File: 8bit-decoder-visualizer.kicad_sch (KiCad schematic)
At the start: 24 parts, among them U1 LED Display Module, U2 LED Display Module, U3 LED Display Module, U4 LED Display Module, U5 LED Display Module, U6 LED Display Module, U7 74HC595

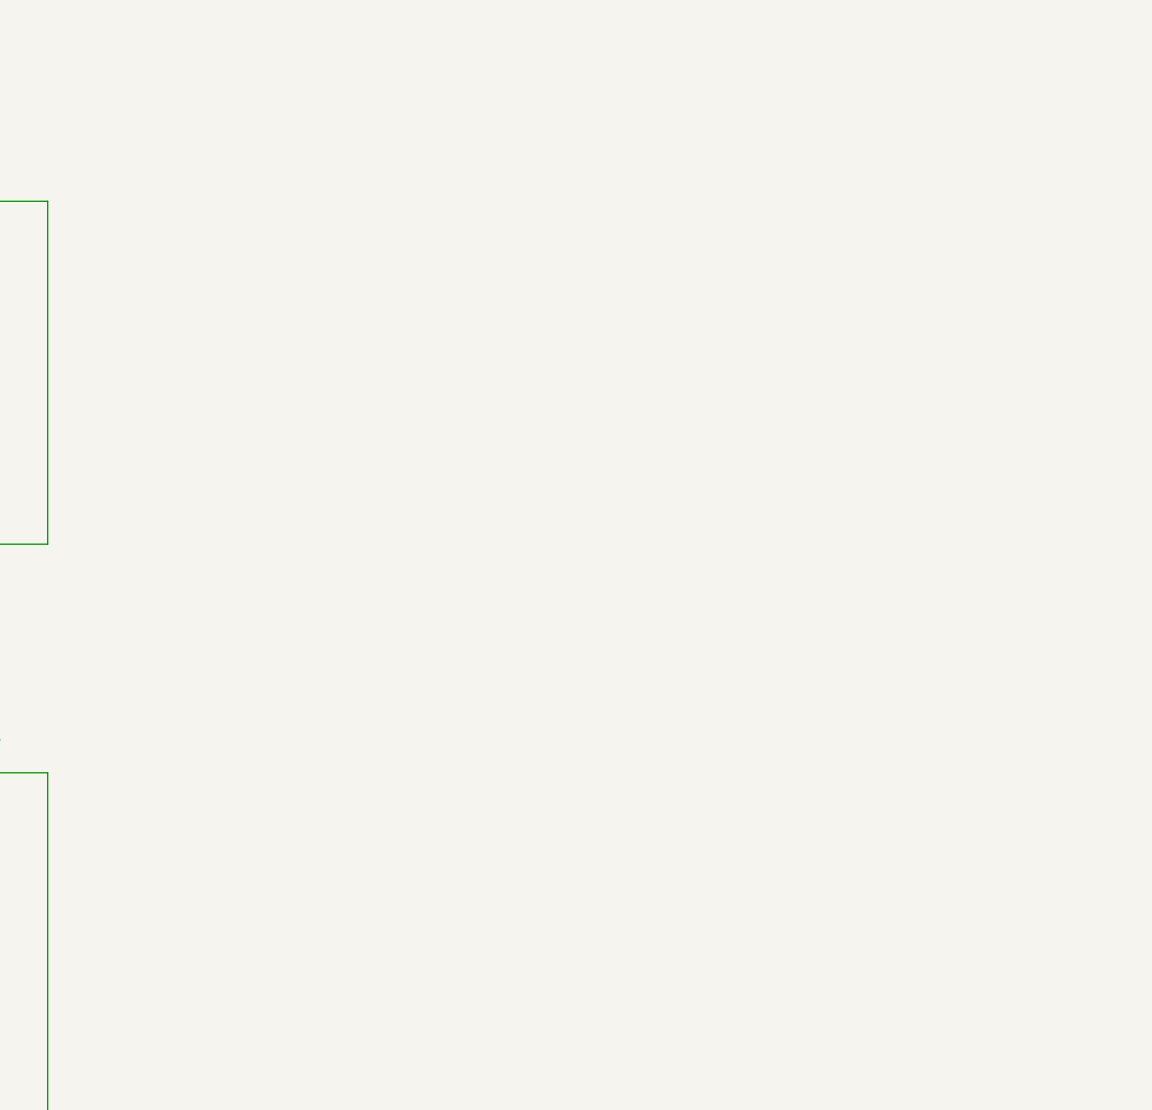
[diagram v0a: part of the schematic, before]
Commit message: xiao との接続以外の回路を書いた
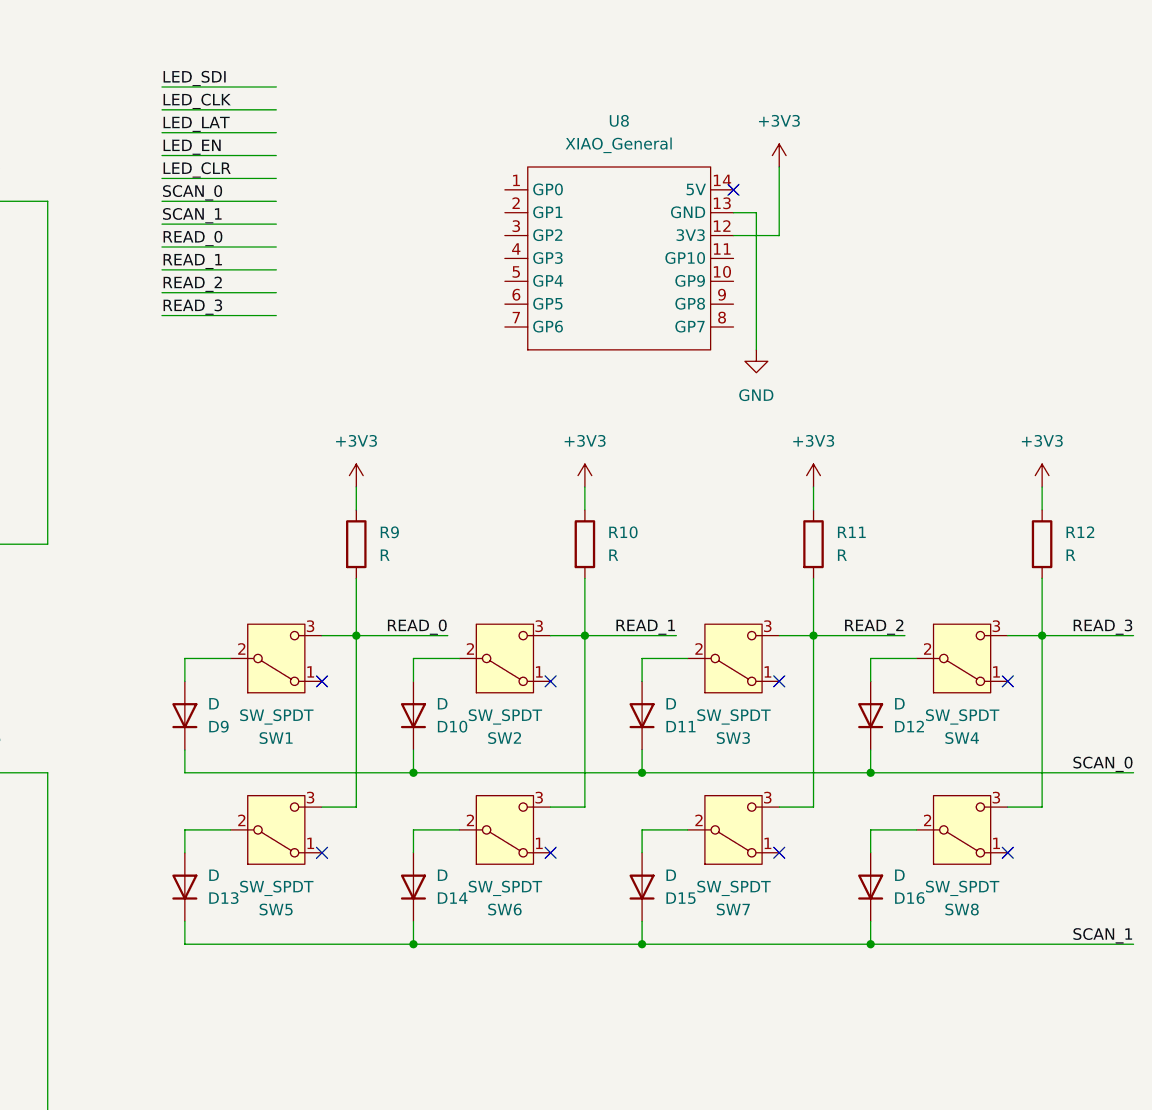
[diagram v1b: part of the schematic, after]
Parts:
- added D10, D11, D12, D13, D14, D15, D16, D9: D, symbol Device:D
- added R10, R11, R12, R9: R, Resistor_SMD:R_0603_1608Metric, symbol Device:R
- added SW1, SW2, SW3, SW4, SW5, SW6, SW7, SW8: SW_SPDT, Button_Switch_THT:SW_Slide_SPDT_Straight_CK_OS102011MS2Q, symbol Switch:SW_SPDT
- added U8: XIAO_General, board:XIAO_ESP32_C3, symbol board:XIAO_General
- U7: footprint (none) -> Package_DIP:DIP-16_W7.62mm
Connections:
- net +3V3: now also R10.1, R11.1, R12.1, R9.1, U8.12 (3V3)
- net GND: now also U8.13 (GND)
- new net: D11.2 (A), SW3.2 (B)
- new net: D12.2 (A), SW4.2 (B)
- new net: D10.2 (A), SW2.2 (B)
- new net: D14.2 (A), SW6.2 (B)
- new net: D15.2 (A), SW7.2 (B)
- new net: D13.2 (A), SW5.2 (B)
- new net: D16.2 (A), SW8.2 (B)
- new net: D9.2 (A), SW1.2 (B)
- new net READ_0: R9.2, SW1.3 (C), SW5.3 (C)
- new net READ_1: R10.2, SW2.3 (C), SW6.3 (C)
- new net READ_2: R11.2, SW3.3 (C), SW7.3 (C)
- new net READ_3: R12.2, SW4.3 (C), SW8.3 (C)
- new net SCAN_0: D10.1 (K), D11.1 (K), D12.1 (K), D9.1 (K)
- new net SCAN_1: D13.1 (K), D14.1 (K), D15.1 (K), D16.1 (K)
- no-connect marks 1 -> 10

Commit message: フットプリントの割り当てを忘れてたでヤンス
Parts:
- D10, D11, D12, D13, D14, D15, D16, D9: footprint (none) -> Diode_SMD:D_SOD-123F
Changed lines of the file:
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@@
 			)
 		)
-		(property "Footprint" ""
+		(property "Footprint" "Diode_SMD:D_SOD-123F"
 			(at 243.84 95.25 0)
 			(effects
@@
 			)
 		)
-		(property "Footprint" ""
+		(property "Footprint" "Diode_SMD:D_SOD-123F"
 			(at 193.04 95.25 0)
 			(effects
@@
 			)
 		)
-		(property "Footprint" ""
+		(property "Footprint" "Diode_SMD:D_SOD-123F"
 			(at 193.04 114.3 0)
 			(effects
@@
 			)
 		)
-		(property "Footprint" ""
+		(property "Footprint" "Diode_SMD:D_SOD-123F"
 			(at 167.64 114.3 0)
 			(effects
@@
 			)
 		)
-		(property "Footprint" ""
+		(property "Footprint" "Diode_SMD:D_SOD-123F"
 			(at 218.44 95.25 0)
 			(effects
@@
 			)
 		)
-		(property "Footprint" ""
+		(property "Footprint" "Diode_SMD:D_SOD-123F"
 			(at 218.44 114.3 0)
 			(effects
@@
 			)
 		)
-		(property "Footprint" ""
+		(property "Footprint" "Diode_SMD:D_SOD-123F"
 			(at 243.84 114.3 0)
 			(effects
@@
 			)
 		)
-		(property "Footprint" ""
+		(property "Footprint" "Diode_SMD:D_SOD-123F"
 			(at 167.64 95.25 0)
 			(effects

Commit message: 未確定の配線を割り当て
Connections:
- net LED_CLK: now also U8.2 (GP1)
- net LED_CLR: now also U8.5 (GP4)
- net LED_EN: now also U8.3 (GP2)
- net LED_LAT: now also U8.4 (GP3)
- net LED_SDI: now also U8.1 (GP0)
- net READ_0: now also U8.11 (GP10)
- net READ_1: now also U8.10 (GP9)
- net READ_2: now also U8.9 (GP8)
- net READ_3: now also U8.8 (GP7)
- net SCAN_0: now also U8.6 (GP5)
- net SCAN_1: now also U8.7 (GP6)
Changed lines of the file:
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@@
 	(wire
 		(pts
-			(xy 165.1 33.02) (xy 177.8 33.02)
+			(xy 190.5 41.91) (xy 203.2 41.91)
 		)
 		(stroke
@@
 	(wire
 		(pts
-			(xy 165.1 43.18) (xy 177.8 43.18)
+			(xy 241.3 44.45) (xy 228.6 44.45)
 		)
 		(stroke
@@
 	(wire
 		(pts
-			(xy 165.1 27.94) (xy 177.8 27.94)
+			(xy 190.5 39.37) (xy 203.2 39.37)
 		)
 		(stroke
@@
 	(wire
 		(pts
-			(xy 165.1 35.56) (xy 177.8 35.56)
+			(xy 190.5 46.99) (xy 203.2 46.99)
 		)
 		(stroke
@@
 	(wire
 		(pts
-			(xy 165.1 38.1) (xy 177.8 38.1)
+			(xy 190.5 49.53) (xy 203.2 49.53)
 		)
 		(stroke
@@
 	(wire
 		(pts
-			(xy 165.1 25.4) (xy 177.8 25.4)
+			(xy 190.5 36.83) (xy 203.2 36.83)
 		)
 		(stroke
@@
 	(wire
 		(pts
-			(xy 165.1 45.72) (xy 177.8 45.72)
+			(xy 241.3 46.99) (xy 228.6 46.99)
 		)
 		(stroke
@@
 	(wire
 		(pts
-			(xy 165.1 50.8) (xy 177.8 50.8)
+			(xy 241.3 52.07) (xy 228.6 52.07)
 		)
 		(stroke
@@
 	(wire
 		(pts
-			(xy 165.1 30.48) (xy 177.8 30.48)
-		)
-		(stroke
-			(width 0)
-			(type default)
-		)
-	)
-	(wire
-		(pts
-			(xy 165.1 40.64) (xy 177.8 40.64)
+			(xy 190.5 44.45) (xy 203.2 44.45)
+		)
+		(stroke
+			(width 0)
+			(type default)
+		)
+	)
+	(wire
+		(pts
+			(xy 190.5 52.07) (xy 203.2 52.07)
 		)
 		(stroke
@@
 	(wire
 		(pts
-			(xy 165.1 48.26) (xy 177.8 48.26)
+			(xy 241.3 49.53) (xy 228.6 49.53)
 		)
 		(stroke
@@
 	)
 	(label "LED_LAT"
-		(at 165.1 30.48 0)
+		(at 190.5 44.45 0)
 		(fields_autoplaced yes)
 		(effects
@@
 	)
 	(label "LED_SDI"
-		(at 165.1 25.4 0)
+		(at 190.5 36.83 0)
 		(fields_autoplaced yes)
 		(effects
@@
 	)
 	(label "LED_EN"
-		(at 165.1 33.02 0)
+		(at 190.5 41.91 0)
 		(fields_autoplaced yes)
 		(effects
@@
 	)
 	(label "READ_1"
-		(at 165.1 45.72 0)
-		(fields_autoplaced yes)
-		(effects
-			(font
-				(size 1.27 1.27)
-			)
-			(justify left bottom)
+		(at 241.3 46.99 180)
+		(fields_autoplaced yes)
+		(effects
+			(font
+				(size 1.27 1.27)
+			)
+			(justify right bottom)
 		)
 	)
@@
 	)
 	(label "READ_3"
-		(at 165.1 50.8 0)
-		(fields_autoplaced yes)
-		(effects
-			(font
-				(size 1.27 1.27)
-			)
-			(justify left bottom)
+		(at 241.3 52.07 180)
+		(fields_autoplaced yes)
+		(effects
+			(font
+				(size 1.27 1.27)
+			)
+			(justify right bottom)
 		)
 	)
@@
 	)
 	(label "SCAN_0"
-		(at 165.1 38.1 0)
+		(at 190.5 49.53 0)
 		(fields_autoplaced yes)
 		(effects
@@
 	)
 	(label "READ_0"
-		(at 165.1 43.18 0)
-		(fields_autoplaced yes)
-		(effects
-			(font
-				(size 1.27 1.27)
-			)
-			(justify left bottom)
+		(at 241.3 44.45 180)
+		(fields_autoplaced yes)
+		(effects
+			(font
+				(size 1.27 1.27)
+			)
+			(justify right bottom)
 		)
 	)
 	(label "READ_2"
-		(at 165.1 48.26 0)
-		(fields_autoplaced yes)
-		(effects
-			(font
-				(size 1.27 1.27)
-			)
-			(justify left bottom)
+		(at 241.3 49.53 180)
+		(fields_autoplaced yes)
+		(effects
+			(font
+				(size 1.27 1.27)
+			)
+			(justify right bottom)
 		)
 	)
 	(label "SCAN_1"
-		(at 165.1 40.64 0)
+		(at 190.5 52.07 0)
 		(fields_autoplaced yes)
 		(effects
@@
 	)
 	(label "LED_CLK"
-		(at 165.1 27.94 0)
+		(at 190.5 39.37 0)
 		(fields_autoplaced yes)
 		(effects
@@
 	)
 	(label "LED_CLR"
-		(at 165.1 35.56 0)
-		(fields_autoplaced yes)
-		(effects
+		(at 190.5 46.99 0)
+		(fields_autoplaced yes)
+		(effects

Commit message: 回路調整
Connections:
- net +3V3: no longer U1.7 (VDD), U2.7 (VDD), U3.7 (VDD), U4.1 (VDD), U4.7 (VDD), U5.1 (VDD), U5.7 (VDD), U6.1 (VDD), U6.7 (VDD)
- net GND: no longer U1.6 (GND), U2.6 (GND), U3.6 (GND), U4.2 (GND), U4.6 (GND), U5.2 (GND), U5.6 (GND), U6.2 (GND), U6.6 (GND)
- new net: U2.7 (VDD), U5.1 (VDD)
- new net: U2.6 (GND), U5.2 (GND)
- new net: U1.6 (GND), U4.2 (GND)
- new net: U1.7 (VDD), U4.1 (VDD)
- new net: U3.6 (GND), U6.2 (GND)
- new net: U3.7 (VDD), U6.1 (VDD)
- no-connect marks 10 -> 16

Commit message: 部品表作った
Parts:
- C1: value C -> 0.1uF
- R1, R2, R3, R4, R5, R6, R7, R8: value R -> 1k
- R10, R11, R12, R9: value R -> 10k
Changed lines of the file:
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@@
 	(label "LED_LAT"
 		(at 190.5 44.45 0)
-		(fields_autoplaced yes)
 		(effects
 			(font
@@
 	(label "LED_EN"
 		(at 64.77 111.76 0)
-		(fields_autoplaced yes)
 		(effects
 			(font
@@
 	(label "LED_SDI"
 		(at 20.32 38.1 0)
-		(fields_autoplaced yes)
 		(effects
 			(font
@@
 	(label "LED_CLR"
 		(at 109.22 50.8 0)
-		(fields_autoplaced yes)
 		(effects
 			(font
@@
 	(label "LED_LAT"
 		(at 109.22 43.18 0)
-		(fields_autoplaced yes)
 		(effects
 			(font
@@
 	(label "LED_CLR"
 		(at 109.22 114.3 0)
-		(fields_autoplaced yes)
 		(effects
 			(font
@@
 	(label "LED_LAT"
 		(at 64.77 106.68 0)
-		(fields_autoplaced yes)
 		(effects
 			(font
@@
 	(label "LED_CLR"
 		(at 64.77 114.3 0)
-		(fields_autoplaced yes)
 		(effects
 			(font
@@
 	(label "LED_CLK"
 		(at 64.77 104.14 0)
-		(fields_autoplaced yes)
 		(effects
 			(font
@@
 	(label "LED_SDI"
 		(at 190.5 36.83 0)
-		(fields_autoplaced yes)
 		(effects
 			(font
@@
 	(label "LED_EN"
 		(at 190.5 41.91 0)
-		(fields_autoplaced yes)
 		(effects
 			(font
@@
 	(label "READ_0"
 		(at 196.85 86.36 180)
-		(fields_autoplaced yes)
 		(effects
 			(font
@@
 	(label "LED_LAT"
 		(at 20.32 43.18 0)
-		(fields_autoplaced yes)
 		(effects
 			(font
@@
 	(label "LED_CLK"
 		(at 109.22 40.64 0)
-		(fields_autoplaced yes)
 		(effects
 			(font
@@
 	(label "READ_1"
 		(at 241.3 46.99 180)
-		(fields_autoplaced yes)
 		(effects
 			(font
@@
 	(label "LED_EN"
 		(at 64.77 48.26 0)
-		(fields_autoplaced yes)
 		(effects
 			(font
@@
 	(label "LED_CLK"
 		(at 22.86 160.02 0)
-		(fields_autoplaced yes)
 		(effects
 			(font
@@
 	(label "LED_EN"
 		(at 20.32 111.76 0)
-		(fields_autoplaced yes)
 		(effects
 			(font
@@
 	(label "LED_EN"
 		(at 22.86 170.18 0)
-		(fields_autoplaced yes)
 		(effects
 			(font
@@
 	(label "LED_LAT"
 		(at 109.22 106.68 0)
-		(fields_autoplaced yes)
 		(effects
 			(font
@@
 	(label "LED_LAT"
 		(at 64.77 43.18 0)
-		(fields_autoplaced yes)
 		(effects
 			(font
@@
 	(label "READ_3"
 		(at 241.3 52.07 180)
-		(fields_autoplaced yes)
 		(effects
 			(font
@@
 	(label "LED_CLR"
 		(at 20.32 114.3 0)
-		(fields_autoplaced yes)
 		(effects
 			(font
@@
 	(label "SCAN_1"
 		(at 273.05 120.65 180)
-		(fields_autoplaced yes)
 		(effects
 			(font
@@
 	(label "READ_2"
 		(at 247.65 86.36 180)
-		(fields_autoplaced yes)
 		(effects
 			(font
@@
 	(label "SCAN_0"
 		(at 190.5 49.53 0)
-		(fields_autoplaced yes)
 		(effects
 			(font
@@
 	(label "READ_0"
 		(at 241.3 44.45 180)
-		(fields_autoplaced yes)
 		(effects
 			(font
@@
 	(label "READ_2"
 		(at 241.3 49.53 180)
-		(fields_autoplaced yes)
 		(effects
 			(font
@@
 	(label "SCAN_1"
 		(at 190.5 52.07 0)
-		(fields_autoplaced yes)
 		(effects
 			(font
@@
 	(label "LED_CLR"
 		(at 20.32 50.8 0)
-		(fields_autoplaced yes)
 		(effects
 			(font
@@
 	(label "LED_CLK"
 		(at 109.22 104.14 0)
-		(fields_autoplaced yes)
 		(effects
 			(font
@@
 	(label "READ_1"
 		(at 222.25 86.36 180)
-		(fields_autoplaced yes)
 		(effects
 			(font
@@
 	(label "LED_EN"
 		(at 109.22 48.26 0)
-		(fields_autoplaced yes)
 		(effects
 			(font
@@
 	(label "LED_CLR"
 		(at 22.86 162.56 0)
-		(fields_autoplaced yes)
 		(effects
 			(font
@@
 	(label "LED_EN"
 		(at 109.22 111.76 0)
-		(fields_autoplaced yes)
 		(effects
 			(font
@@
 	(label "LED_LAT"
 		(at 22.86 167.64 0)
-		(fields_autoplaced yes)
 		(effects
 			(font
@@
 	(label "READ_3"
 		(at 273.05 86.36 180)
-		(fields_autoplaced yes)
 		(effects
 			(font
@@
 	(label "SCAN_0"
 		(at 273.05 101.6 180)
-		(fields_autoplaced yes)
 		(effects
 			(font
@@
 	(label "LED_CLK"
 		(at 190.5 39.37 0)
-		(fields_autoplaced yes)
 		(effects
 			(font
@@
 	(label "LED_CLR"
 		(at 64.77 50.8 0)
-		(fields_autoplaced yes)
 		(effects
 			(font
@@
 	(label "LED_CLK"
 		(at 64.77 40.64 0)
-		(fields_autoplaced yes)
 		(effects
 			(font
@@
 	(label "LED_CLK"
 		(at 20.32 40.64 0)
-		(fields_autoplaced yes)
 		(effects
 			(font
@@
 	(label "LED_LAT"
 		(at 20.32 106.68 0)
-		(fields_autoplaced yes)
 		(effects
 			(font
@@
 	(label "LED_CLR"
 		(at 190.5 46.99 0)
-		(fields_autoplaced yes)
 		(effects
 			(font
@@
 	(label "LED_CLK"
 		(at 20.32 104.14 0)
-		(fields_autoplaced yes)
 		(effects
 			(font
@@
 	(label "LED_EN"
 		(at 20.32 48.26 0)
-		(fields_autoplaced yes)
 		(effects
 			(font
@@
 			)
 		)
-		(property "Value" "C"
+		(property "Value" "0.1uF"
 			(at 99.06 166.3699 0)
 			(effects
@@
 			)
 		)
-		(property "Value" "R"
+		(property "Value" "10k"
 			(at 189.23 77.4699 0)
 			(effects
@@
 			)
 		)
-		(property "Value" "R"
+		(property "Value" "1k"
 			(at 63.5 158.75 90)
 			(effects
@@
 			)
 		)
-		(property "Value" "R"
+		(property "Value" "10k"
 			(at 240.03 77.4699 0)
 			(effects
@@
 			)
 		)
-		(property "Value" "R"
+		(property "Value" "1k"
 			(at 63.5 168.91 90)
 			(effects
@@
 			)
 		)
-		(property "Value" "R"
+		(property "Value" "10k"
 			(at 214.63 77.4699 0)
 			(effects
@@
 			)
 		)
-		(property "Value" "R"
+		(property "Value" "1k"
 			(at 63.5 166.37 90)
 			(effects
@@
 			)
 		)
-		(property "Value" "R"
+		(property "Value" "1k"
 			(at 63.5 161.29 90)
 			(effects
@@
 			)
 		)
-		(property "Value" "R"
+		(property "Value" "1k"
 			(at 63.5 156.21 90)
 			(effects
@@
 			)
 		)
-		(property "Value" "R"
+		(property "Value" "1k"
 			(at 63.5 153.67 90)
 			(effects
@@
 			)
 		)
-		(property "Value" "R"
+		(property "Value" "1k"
 			(at 63.5 151.13 90)
 			(effects
@@
 			)
 		)
-		(property "Value" "R"
+		(property "Value" "1k"
 			(at 63.5 163.83 90)
 			(effects
@@
 			)
 		)
-		(property "Value" "R"
+		(property "Value" "10k"
 			(at 265.43 77.4699 0)
 			(effects

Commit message: いらない LED を消してスイッチのフットプリントを修正し、Rev.2 とする
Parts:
- removed U4: LED Display Module, display:LED_Display_Module, symbol display:LED_Driver_Module
- SW1, SW2, SW3, SW4, SW5, SW6, SW7, SW8: footprint Button_Switch_THT:SW_Slide_SPDT_Straight_CK_OS102011MS2Q -> sw:SW_SPDT_100300
- renumbered U5 to U4, U6 to U5, U7 to U6, U8 to U7
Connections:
- net at U4.4 (SDI): now also U3.5 (SDO)
